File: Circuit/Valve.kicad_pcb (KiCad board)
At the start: 2 copper layers, 96.5 x 63.5 mm, 22 parts, among them CN1 GROVE, CN2 ST-LINK, CN3 TTL-232R-3V3, J1 Conn_01x04_Male, SW1 RESET, U1 STM32L010F4P6

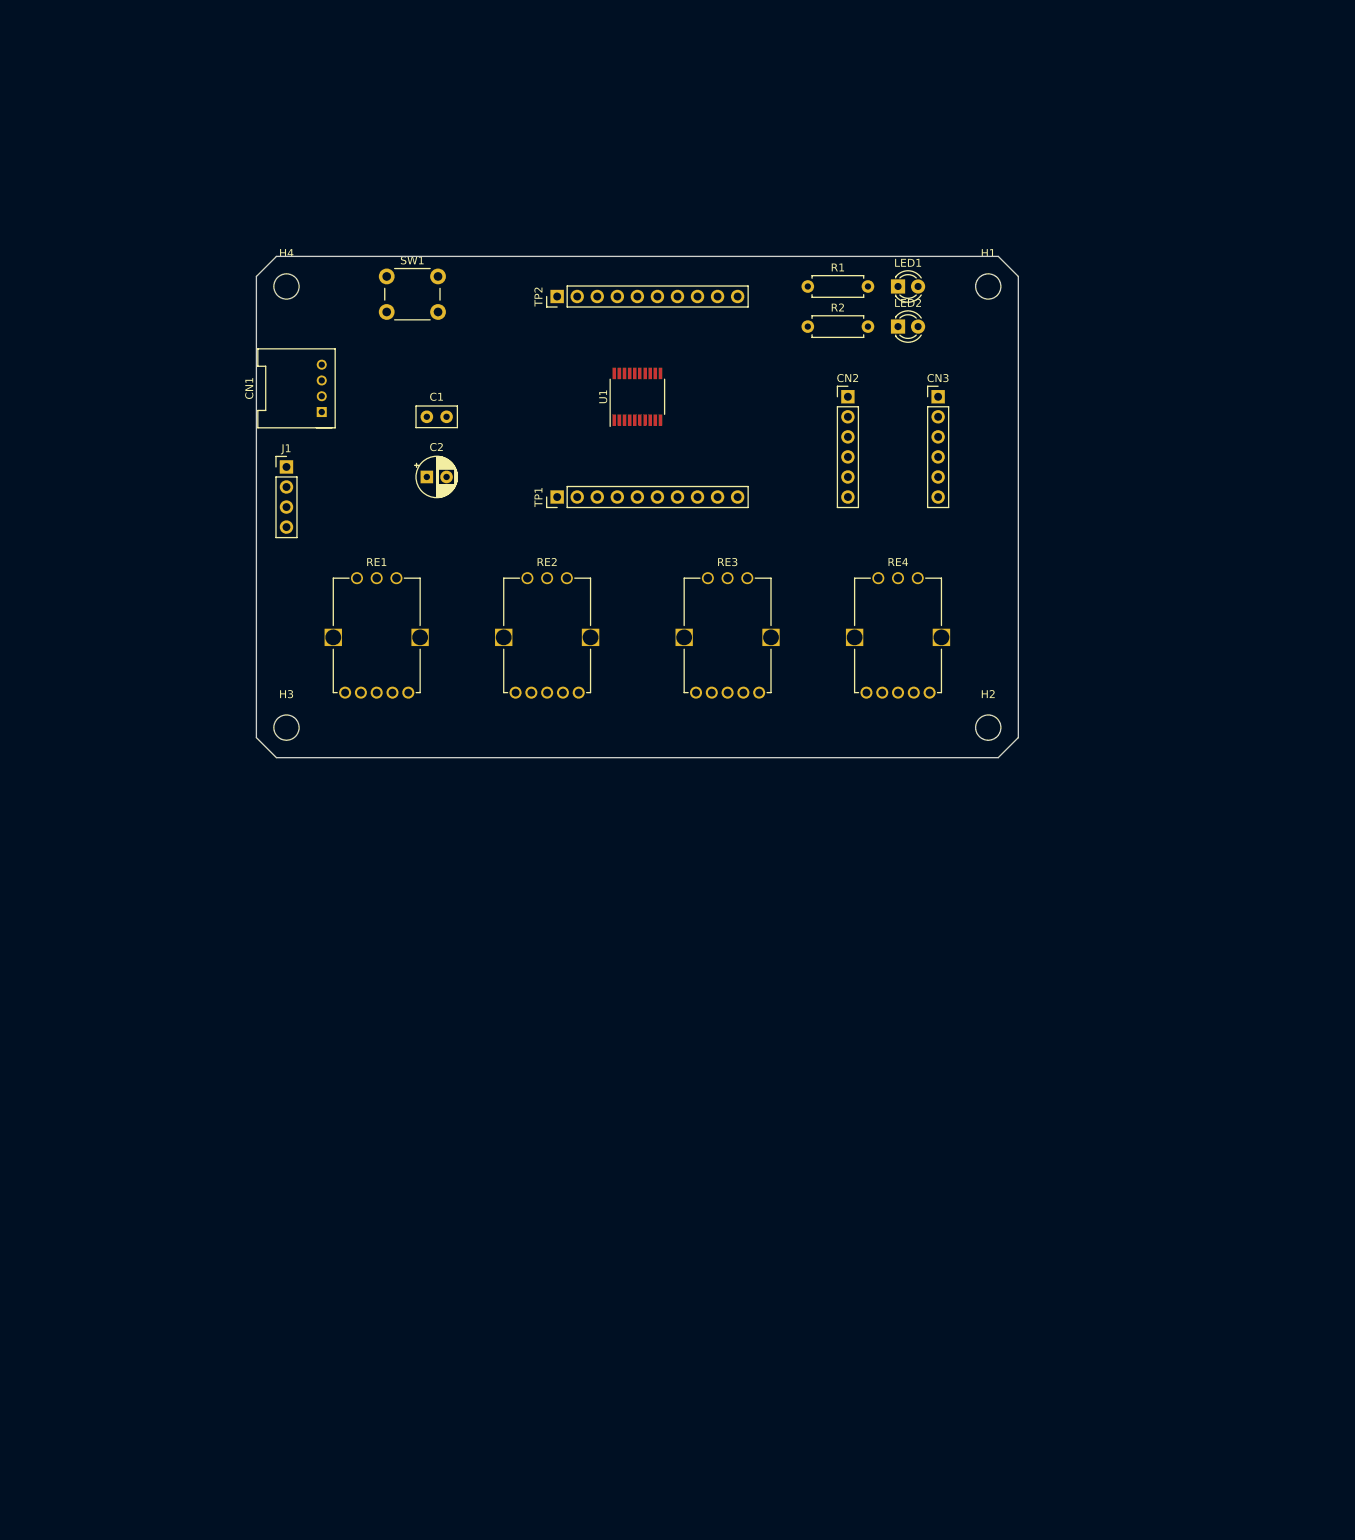
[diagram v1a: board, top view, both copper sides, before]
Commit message: フットプリントにB基板外形を記載
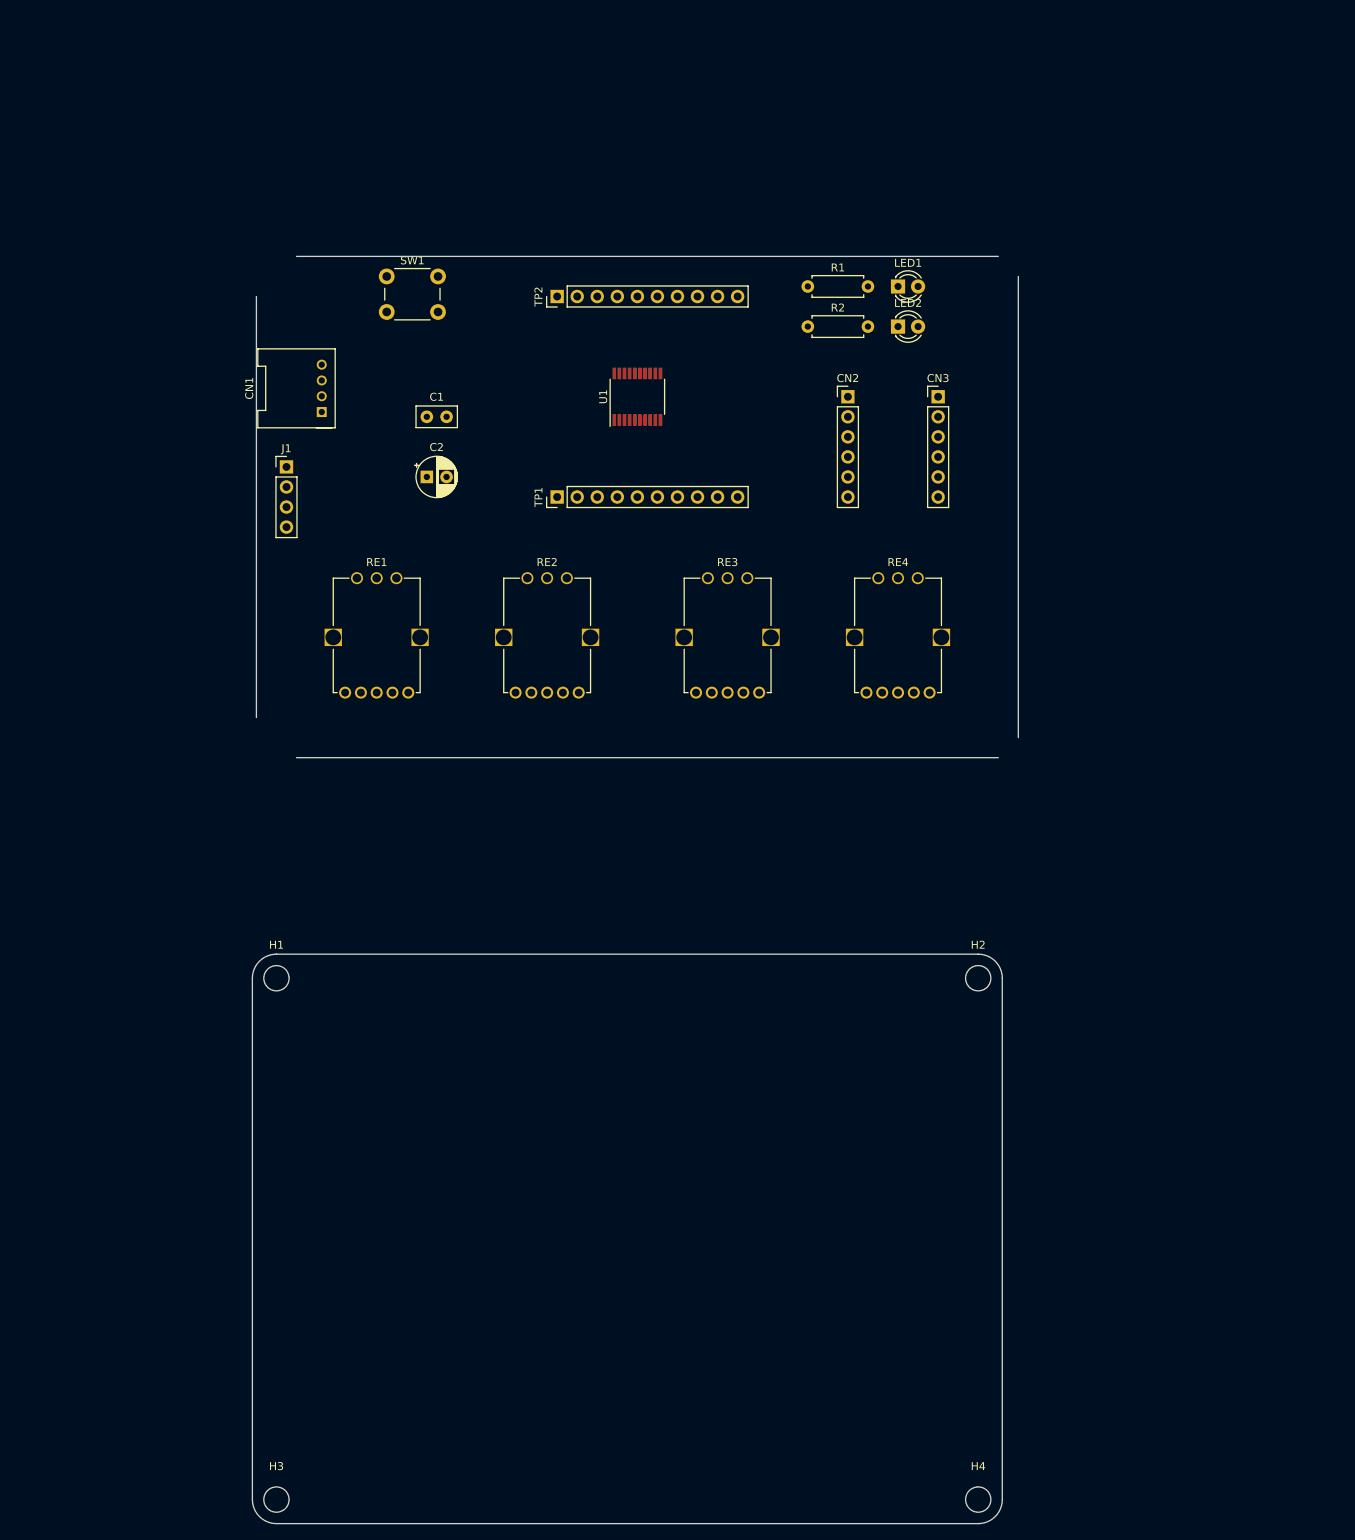
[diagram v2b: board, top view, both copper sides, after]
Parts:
- moved H4 176.9 mm to (165.1, 205.7)
- moved H1 125.7 mm to (76.2, 139.7)
- moved H3 97.8 mm to (76.2, 205.7)
- moved H2 31.8 mm to (165.1, 139.7)
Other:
- board size 96.5 x 63.5 mm -> 97 x 160.5 mm
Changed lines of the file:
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@@
   (general
     (thickness 1.6)
-    (drawings 16)
+    (drawings 30)
     (tracks 0)
     (zones 0)
@@
   )
   (module MountingHole:MountingHole_3.2mm_M3 (layer F.Cu)
-    (at 166.37 52.07)
+    (at 76.2 139.7)
     (descr "Mounting Hole 3.2mm, no annular, M3")
     (tags "mounting hole 3.2mm no annular m3")
@@
   )
   (module MountingHole:MountingHole_3.2mm_M3 (layer F.Cu)
-    (at 166.37 107.95)
+    (at 165.1 139.7)
     (descr "Mounting Hole 3.2mm, no annular, M3")
     (tags "mounting hole 3.2mm no annular m3")
@@
   )
   (module MountingHole:MountingHole_3.2mm_M3 (layer F.Cu)
-    (at 77.47 107.95)
+    (at 76.2 205.74)
     (descr "Mounting Hole 3.2mm, no annular, M3")
     (tags "mounting hole 3.2mm no annular m3")
@@
   )
   (module MountingHole:MountingHole_3.2mm_M3 (layer F.Cu)
-    (at 77.47 52.07)
+    (at 165.1 205.74)
     (descr "Mounting Hole 3.2mm, no annular, M3")
     (tags "mounting hole 3.2mm no annular m3")
@@
     )
   )
-  (gr_line (start 73.66 50.8) (end 76.2 48.26) (layer Edge.Cuts) (width 0.15))
-  (gr_line (start 167.64 48.26) (end 170.18 50.8) (layer Edge.Cuts) (width 0.15))
-  (gr_line (start 167.64 111.76) (end 170.18 109.22) (layer Edge.Cuts) (width 0.15))
-  (gr_line (start 73.66 109.22) (end 76.2 111.76) (layer Edge.Cuts) (width 0.15))
+  (dimension 72.136 (width 0.3) (layer F.Fab)
+    (gr_text "72.136 mm (About 72)" (at 190.94 172.72 270) (layer F.Fab)
+      (effects (font (size 1.5 1.5) (thickness 0.3)))
+    )
+    (feature1 (pts (xy 193.04 208.788) (xy 192.453579 208.788)))
+    (feature2 (pts (xy 193.04 136.652) (xy 192.453579 136.652)))
+    (crossbar (pts (xy 193.04 136.652) (xy 193.04 208.788)))
+    (arrow1a (pts (xy 193.04 208.788) (xy 192.453579 207.661496)))
+    (arrow1b (pts (xy 193.04 208.788) (xy 193.626421 207.661496)))
+    (arrow2a (pts (xy 193.04 136.652) (xy 192.453579 137.778504)))
+    (arrow2b (pts (xy 193.04 136.652) (xy 193.626421 137.778504)))
+  )
+  (dimension 3.048 (width 0.3) (layer F.Fab)
+    (gr_text "3.048 mm" (at 180.78 207.264 270) (layer F.Fab)
+      (effects (font (size 1.5 1.5) (thickness 0.3)))
+    )
+    (feature1 (pts (xy 182.88 208.788) (xy 182.293579 208.788)))
+    (feature2 (pts (xy 182.88 205.74) (xy 182.293579 205.74)))
+    (crossbar (pts (xy 182.88 205.74) (xy 182.88 208.788)))
+    (arrow1a (pts (xy 182.88 208.788) (xy 182.293579 207.661496)))
+    (arrow1b (pts (xy 182.88 208.788) (xy 183.466421 207.661496)))
+    (arrow2a (pts (xy 182.88 205.74) (xy 182.293579 206.866504)))
+    (arrow2b (pts (xy 182.88 205.74) (xy 183.466421 206.866504)))
+  )
+  (dimension 3.048 (width 0.3) (layer F.Fab)
+    (gr_text "3.048 mm" (at 180.78 138.176 270) (layer F.Fab)
+      (effects (font (size 1.5 1.5) (thickness 0.3)))
+    )
+    (feature1 (pts (xy 182.88 139.7) (xy 182.293579 139.7)))
+    (feature2 (pts (xy 182.88 136.652) (xy 182.293579 136.652)))
+    (crossbar (pts (xy 182.88 136.652) (xy 182.88 139.7)))
+    (arrow1a (pts (xy 182.88 139.7) (xy 182.293579 138.573496)))
+    (arrow1b (pts (xy 182.88 139.7) (xy 183.466421 138.573496)))
+    (arrow2a (pts (xy 182.88 136.652) (xy 182.293579 137.778504)))
+    (arrow2b (pts (xy 182.88 136.652) (xy 183.466421 137.778504)))
+  )
+  (dimension 3.048 (width 0.3) (layer F.Fab)
+    (gr_text "3.048 mm" (at 166.624 218) (layer F.Fab)
+      (effects (font (size 1.5 1.5) (thickness 0.3)))
+    )
+    (feature1 (pts (xy 168.148 215.9) (xy 168.148 216.486421)))
+    (feature2 (pts (xy 165.1 215.9) (xy 165.1 216.486421)))
+    (crossbar (pts (xy 165.1 215.9) (xy 168.148 215.9)))
+    (arrow1a (pts (xy 168.148 215.9) (xy 167.021496 216.486421)))
+    (arrow1b (pts (xy 168.148 215.9) (xy 167.021496 215.313579)))
+    (arrow2a (pts (xy 165.1 215.9) (xy 166.226504 216.486421)))
+    (arrow2b (pts (xy 165.1 215.9) (xy 166.226504 215.313579)))
+  )
+  (dimension 94.996 (width 0.3) (layer F.Fab)
+    (gr_text "94.996 mm (About 95)" (at 120.65 230.378955) (layer F.Fab)
+      (effects (font (size 1.5 1.5) (thickness 0.3)))
+    )
+    (feature1 (pts (xy 168.148 228.278955) (xy 168.148 228.865376)))
+    (feature2 (pts (xy 73.152 228.278955) (xy 73.152 228.865376)))
+    (crossbar (pts (xy 73.152 228.278955) (xy 168.148 228.278955)))
+    (arrow1a (pts (xy 168.148 228.278955) (xy 167.021496 228.865376)))
+    (arrow1b (pts (xy 168.148 228.278955) (xy 167.021496 227.692534)))
+    (arrow2a (pts (xy 73.152 228.278955) (xy 74.278504 228.865376)))
+    (arrow2b (pts (xy 73.152 228.278955) (xy 74.278504 227.692534)))
+  )
+  (dimension 3.048 (width 0.3) (layer F.Fab)
+    (gr_text "3.048 mm" (at 74.676 218) (layer F.Fab)
+      (effects (font (size 1.5 1.5) (thickness 0.3)))
+    )
+    (feature1 (pts (xy 76.2 215.9) (xy 76.2 216.486421)))
+    (feature2 (pts (xy 73.152 215.9) (xy 73.152 216.486421)))
+    (crossbar (pts (xy 73.152 215.9) (xy 76.2 215.9)))
+    (arrow1a (pts (xy 76.2 215.9) (xy 75.073496 216.486421)))
+    (arrow1b (pts (xy 76.2 215.9) (xy 75.073496 215.313579)))
+    (arrow2a (pts (xy 73.152 215.9) (xy 74.278504 216.486421)))
+    (arrow2b (pts (xy 73.152 215.9) (xy 74.278504 215.313579)))
+  )
+  (dimension 66.04 (width 0.3) (layer F.Fab)
+    (gr_text "66.040 mm (About 66)" (at 180.78 172.72 270) (layer F.Fab)
+      (effects (font (size 1.5 1.5) (thickness 0.3)))
+    )
+    (feature1 (pts (xy 182.88 205.74) (xy 182.293579 205.74)))
+    (feature2 (pts (xy 182.88 139.7) (xy 182.293579 139.7)))
+    (crossbar (pts (xy 182.88 139.7) (xy 182.88 205.74)))
+    (arrow1a (pts (xy 182.88 205.74) (xy 182.293579 204.613496)))
+    (arrow1b (pts (xy 182.88 205.74) (xy 183.466421 204.613496)))
+    (arrow2a (pts (xy 182.88 139.7) (xy 182.293579 140.826504)))
+    (arrow2b (pts (xy 182.88 139.7) (xy 183.466421 140.826504)))
+  )
+  (dimension 88.9 (width 0.3) (layer F.Fab)
+    (gr_text "88.900 mm (About 89)" (at 120.65 218) (layer F.Fab)
+      (effects (font (size 1.5 1.5) (thickness 0.3)))
+    )
+    (feature1 (pts (xy 165.1 215.9) (xy 165.1 216.486421)))
+    (feature2 (pts (xy 76.2 215.9) (xy 76.2 216.486421)))
+    (crossbar (pts (xy 76.2 215.9) (xy 165.1 215.9)))
+    (arrow1a (pts (xy 165.1 215.9) (xy 163.973496 216.486421)))
+    (arrow1b (pts (xy 165.1 215.9) (xy 163.973496 215.313579)))
+    (arrow2a (pts (xy 76.2 215.9) (xy 77.326504 216.486421)))
+    (arrow2b (pts (xy 76.2 215.9) (xy 77.326504 215.313579)))
+  )
+  (gr_arc (start 165.1 205.74) (end 165.1 208.788) (angle -90) (layer Edge.Cuts) (width 0.15))
+  (gr_arc (start 165.1 139.7) (end 168.148 139.7) (angle -90) (layer Edge.Cuts) (width 0.15))
+  (gr_arc (start 76.2 139.7) (end 76.2 136.652) (angle -90) (layer Edge.Cuts) (width 0.15))
+  (gr_arc (start 76.2 205.74) (end 73.152 205.74) (angle -90) (layer Edge.Cuts) (width 0.15))
+  (gr_line (start 165.1 136.652) (end 76.2 136.652) (layer Edge.Cuts) (width 0.15))
+  (gr_line (start 168.148 205.74) (end 168.148 139.7) (layer Edge.Cuts) (width 0.15))
+  (gr_line (start 73.152 205.74) (end 73.152 139.7) (layer Edge.Cuts) (width 0.15))
+  (gr_line (start 76.2 208.788) (end 165.1 208.788) (layer Edge.Cuts) (width 0.15))
+  (gr_line (start 165.1 139.7) (end 76.2 139.7) (layer F.Fab) (width 0.2))
+  (gr_line (start 165.1 205.74) (end 165.1 139.7) (layer F.Fab) (width 0.2))
+  (gr_line (start 76.2 205.74) (end 165.1 205.74) (layer F.Fab) (width 0.2))
+  (gr_line (start 76.2 139.7) (end 76.2 205.74) (layer F.Fab) (width 0.2))
   (dimension 21.59 (width 0.3) (layer F.Fab)
     (gr_text "21.590 mm" (at 144.145 108.78) (layer F.Fab)
@@
     (arrow2b (pts (xy 167.814672 117.342868) (xy 166.688168 117.929289)))
   )
-  (dimension 91.44 (width 0.3) (layer F.Fab)
-    (gr_text "91.440 mm" (at 121.92 127.83) (layer F.Fab)
-      (effects (font (size 1.5 1.5) (thickness 0.3)))
-    )
-    (feature1 (pts (xy 76.2 124.46) (xy 76.2 126.316421)))
-    (feature2 (pts (xy 167.64 124.46) (xy 167.64 126.316421)))
-    (crossbar (pts (xy 167.64 125.73) (xy 76.2 125.73)))
-    (arrow1a (pts (xy 76.2 125.73) (xy 77.326504 125.143579)))
-    (arrow1b (pts (xy 76.2 125.73) (xy 77.326504 126.316421)))
-    (arrow2a (pts (xy 167.64 125.73) (xy 166.513496 125.143579)))
-    (arrow2b (pts (xy 167.64 125.73) (xy 166.513496 126.316421)))
-  )
-  (gr_line (start 121.92 114.3) (end 121.92 121.92) (layer F.Fab) (width 0.2))
-  (gr_line (start 167.64 48.26) (end 76.2 48.26) (layer Edge.Cuts) (width 0.15))
+  (gr_line (start 167.64 48.26) (end 78.74 48.26) (layer Edge.Cuts) (width 0.15))
   (gr_line (start 170.18 50.8) (end 170.18 50.8) (layer Edge.Cuts) (width 0.15))
   (gr_line (start 170.18 109.22) (end 170.18 50.8) (layer Edge.Cuts) (width 0.15))
-  (gr_line (start 167.64 111.76) (end 76.2 111.76) (layer Edge.Cuts) (width 0.15))
-  (gr_line (start 73.66 50.8) (end 73.66 109.22) (layer Edge.Cuts) (width 0.15))
+  (gr_line (start 167.64 111.76) (end 78.74 111.76) (layer Edge.Cuts) (width 0.15))
+  (gr_line (start 73.66 53.34) (end 73.66 106.68) (layer Edge.Cuts) (width 0.15))
 )

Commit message: B基板外形状に部品仮置き
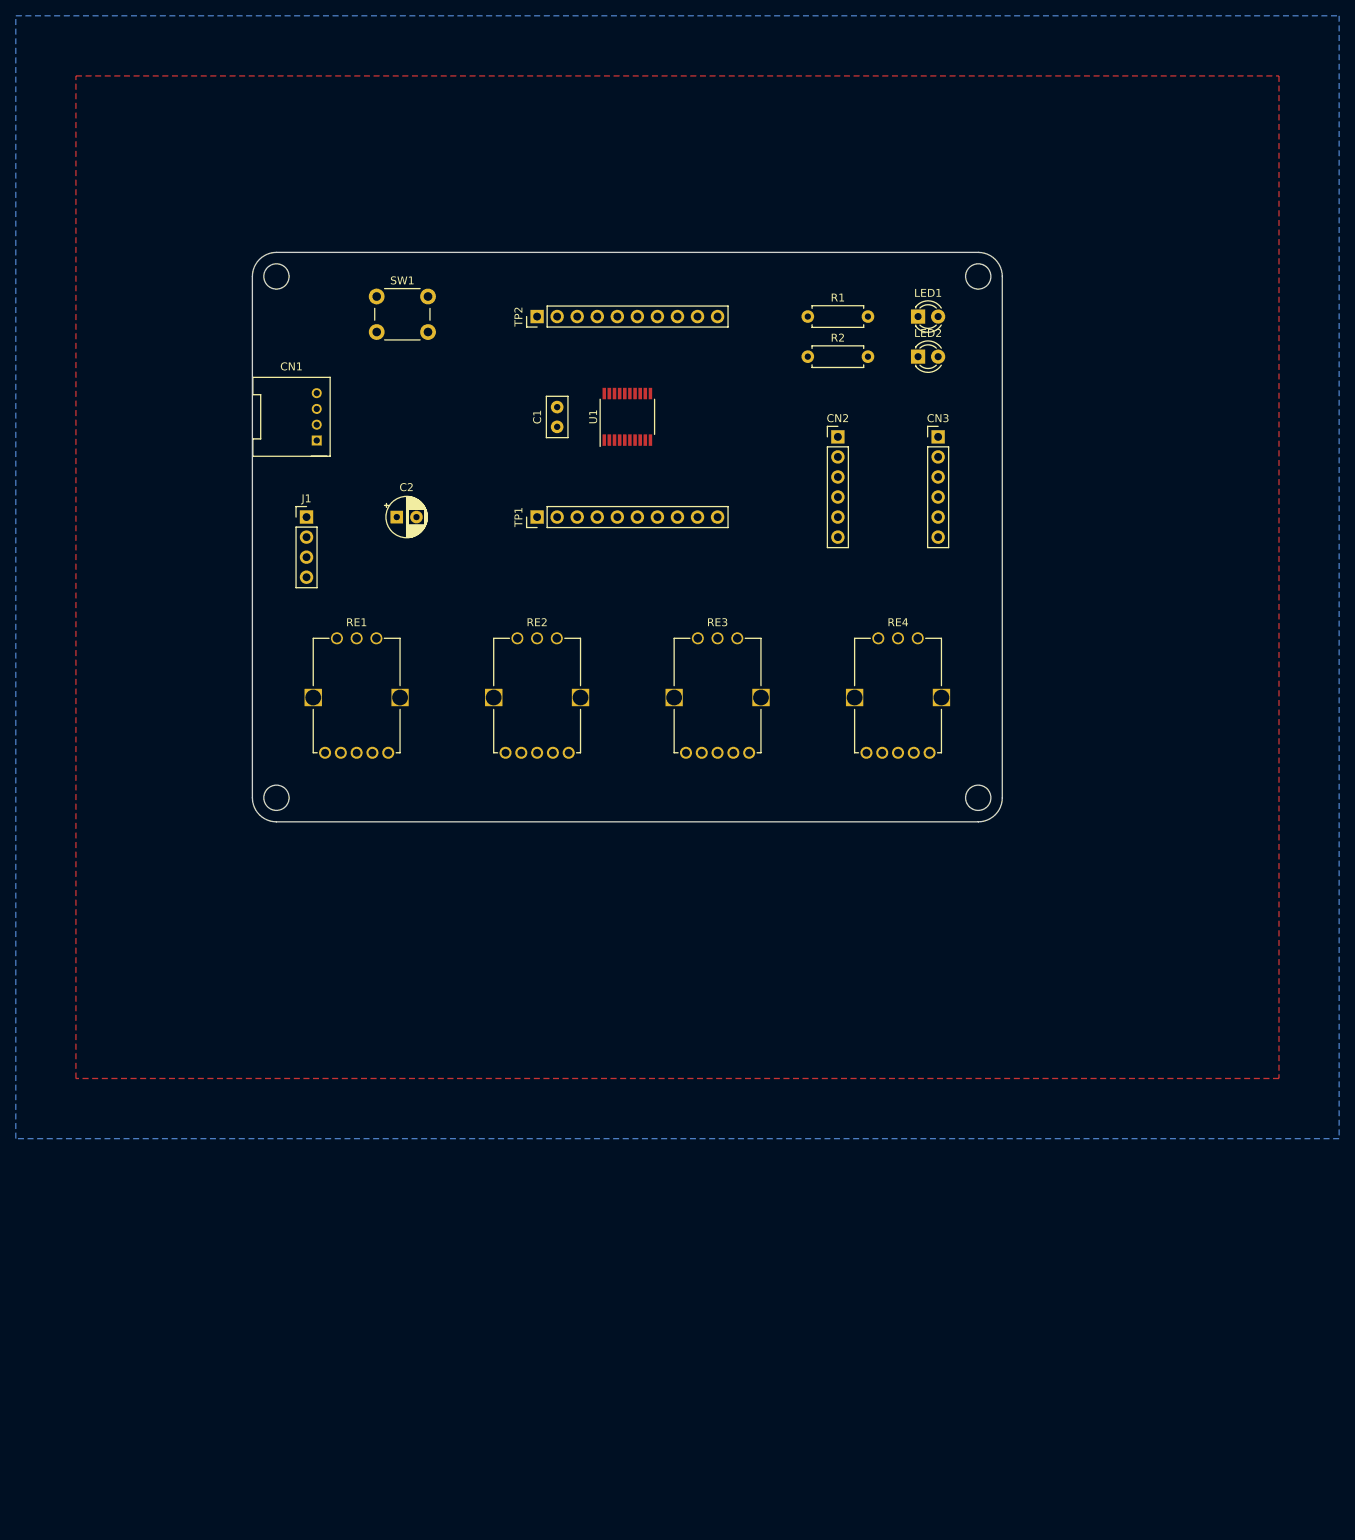
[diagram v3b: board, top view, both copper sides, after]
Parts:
- moved H3 88.9 mm to (76.2, 116.8)
- moved H4 88.9 mm to (165.1, 116.8)
- moved H1 88.9 mm to (76.2, 50.8)
- moved H2 88.9 mm to (165.1, 50.8)
- moved C1 16.6 mm to (111.8, 69.8), turned to 90 degrees
- moved RE1 8.03 mm to (86.4, 104.1)
- moved RE2 7.73 mm to (109.2, 104.1)
- moved RE3 7.73 mm to (132.1, 104.1)
- moved RE4 7.62 mm to (154.9, 104.1)
- moved J1 6.84 mm to (80.0, 81.3)
- moved C2 6.35 mm to (91.4, 81.3)
- moved CN2 5.24 mm to (147.3, 71.1)
- moved CN3 5.08 mm to (160.0, 71.1)
- moved LED1 4.58 mm to (157.5, 55.9)
- moved LED2 4.58 mm to (157.5, 61.0)
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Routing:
- added copper zone on B.Cu, net GND
- added copper zone on F.Cu, net GND
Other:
- board size 97 x 160.5 mm -> 95 x 72.1 mm
